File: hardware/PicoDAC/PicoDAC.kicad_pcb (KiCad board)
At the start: 4 copper layers, 38.6 x 73.3 mm, 48 parts, among them CN1 PJ-327A 5JJ, U1 CS43131-CNZR, U2 XIAO-RP2350-DIP, U3 PCA9306DCUR, U4 SN74AXC4T245PWR, U5 XTPS7A2018, U7 74AHCT1G125GV

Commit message: pcb rev 1.4, final touches
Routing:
- net VBUS: track 61.5 -> 75.5 mm, vias 0 -> 1
- net /USB_GND: track 13.4 -> 15.5 mm
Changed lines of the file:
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@@
 	)
 	(segment
+		(start 150.0227 149.157738)
+		(end 149.464162 148.5992)
+		(width 0.25)
+		(layer "B.Cu")
+		(net 1)
+	)
+	(segment
+		(start 149.464162 148.5992)
+		(end 149.2568 148.5992)
+		(width 0.25)
+		(layer "B.Cu")
+		(net 1)
+	)
+	(segment
+		(start 150.0227 150.219738)
+		(end 150.0227 149.157738)
+		(width 0.25)
+		(layer "B.Cu")
+		(net 1)
+	)
+	(segment
 		(start 156.922662 150.059738)
 		(end 157.3848 149.5976)
@@
 	(via
 		(at 148.25 115.61)
-		(size 0.3)
-		(drill 0.15)
+		(size 0.4)
+		(drill 0.2)
 		(layers "F.Cu" "B.Cu")
 		(net 27)
@@
 	(via
 		(at 149.479397 116.8786)
-		(size 0.3)
-		(drill 0.15)
+		(size 0.4)
+		(drill 0.2)
 		(layers "F.Cu" "B.Cu")
 		(net 27)
@@
 	(via
 		(at 148.229397 118.1286)
-		(size 0.3)
-		(drill 0.15)
+		(size 0.4)
+		(drill 0.2)
 		(layers "F.Cu" "B.Cu")
 		(net 27)
@@
 	(via
 		(at 148.229397 116.8786)
-		(size 0.3)
-		(drill 0.15)
+		(size 0.4)
+		(drill 0.2)
 		(layers "F.Cu" "B.Cu")
 		(net 27)
@@
 	(via
 		(at 149.479397 115.6286)
-		(size 0.3)
-		(drill 0.15)
+		(size 0.4)
+		(drill 0.2)
 		(layers "F.Cu" "B.Cu")
 		(net 27)
@@
 	(via
 		(at 150.729397 115.6286)
-		(size 0.3)
-		(drill 0.15)
+		(size 0.4)
+		(drill 0.2)
 		(layers "F.Cu" "B.Cu")
 		(net 27)
@@
 	(via
 		(at 149.479397 118.1286)
-		(size 0.3)
-		(drill 0.15)
+		(size 0.4)
+		(drill 0.2)
 		(layers "F.Cu" "B.Cu")
 		(net 27)
@@
 	(via
 		(at 150.729397 116.8786)
-		(size 0.3)
-		(drill 0.15)
+		(size 0.4)
+		(drill 0.2)
 		(layers "F.Cu" "B.Cu")
 		(net 27)
@@
 	(via
 		(at 150.729397 118.1286)
-		(size 0.3)
-		(drill 0.15)
+		(size 0.4)
+		(drill 0.2)
 		(layers "F.Cu" "B.Cu")
 		(net 27)
@@
 	)
 	(segment
+		(start 161.165763 88.775763)
+		(end 159.385 86.995)
+		(width 0.5)
+		(layer "F.Cu")
+		(net 68)
+	)
+	(segment
+		(start 162.358 88.775763)
+		(end 161.165763 88.775763)
+		(width 0.5)
+		(layer "F.Cu")
+		(net 68)
+	)
+	(segment
 		(start 161.2982 114.1026)
 		(end 161.2982 110.4882)
@@
 		(net 68)
 	)
+	(via
+		(at 159.385 86.995)
+		(size 0.6)
+		(drill 0.3)
+		(layers "F.Cu" "B.Cu")
+		(net 68)
+	)
+	(segment
+		(start 151.629453 82.804)
+		(end 151.587953 82.7625)
+		(width 1.25)
+		(layer "B.Cu")
+		(net 68)
+	)
+	(segment
+		(start 159.385 86.995)
+		(end 159.385 85.725)
+		(width 1.25)
+		(layer "B.Cu")
+		(net 68)
+	)
+	(segment
+		(start 159.385 85.725)
+		(end 156.464 82.804)
+		(width 1.25)
+		(layer "B.Cu")
+		(net 68)
+	)
+	(segment
+		(start 156.464 82.804)
+		(end 151.629453 82.804)
+		(width 1.25)
+		(layer "B.Cu")
+		(net 68)
+	)
 	(segment
 		(start 150.743053 99.6324)
@@
 	)
 	(zone
-		(net 44)
-		(net_name "/DAC_RESET")
+		(net 9)
+		(net_name "/LED_CONTROL")
 		(layer "F.Cu")
 		(name "$teardrop_padvia$")
 		(hatch none 0.1)
-		(priority 30000)
+		(priority 30005)
 		(attr
 			(teardrop
@@
 		(polygon
 			(pts
-				(xy 153.496991 94.400092) (xy 153.850545 94.046538) (xy 153.538953 93.01087) (xy 152.372246 92.921793)
-				(xy 152.057323 93.6845)
+				(xy 136.278545 81.638462) (xy 135.924991 81.284908) (xy 135.053536 82.0005) (xy 135.562246 82.763207)
+				(xy 136.684316 82.045137)
 			)
 		)
 	)
 	(zone
-		(net 9)
-		(net_name "/LED_CONTROL")
+		(net 44)
+		(net_name "/DAC_RESET")
 		(layer "F.Cu")
 		(name "$teardrop_padvia$")
 		(hatch none 0.1)
-		(priority 30004)
+		(priority 30000)
 		(attr
 			(teardrop
@@
 		(polygon
 			(pts
-				(xy 136.278545 81.638462) (xy 135.924991 81.284908) (xy 135.053536 82.0005) (xy 135.562246 82.763207)
-				(xy 136.684316 82.045137)
+				(xy 153.496991 94.400092) (xy 153.850545 94.046538) (xy 153.538953 93.01087) (xy 152.372246 92.921793)
+				(xy 152.057323 93.6845)
 			)
 		)
 	)
 	(zone
-		(net 9)
-		(net_name "/LED_CONTROL")
+		(net 65)
+		(net_name "/MCU_GP_00")
 		(layer "F.Cu")
 		(name "$teardrop_padvia$")
 		(hatch none 0.1)
-		(priority 30005)
+		(priority 30006)
 		(attr
 			(teardrop
@@
 		(polygon
 			(pts
-				(xy 136.278545 81.638462) (xy 135.924991 81.284908) (xy 135.053536 82.0005) (xy 135.562246 82.763207)
-				(xy 136.684316 82.045137)
+				(xy 135.925859 99.426235) (xy 136.102635 99.249459) (xy 136.621667 98.755525) (xy 135.562246 98.001793)
+				(xy 135.015851 98.7645)
 			)
 		)
 	)
 	(zone
-		(net 65)
-		(net_name "/MCU_GP_00")
+		(net 45)
+		(net_name "/LS1_1OE")
 		(layer "F.Cu")
 		(name "$teardrop_padvia$")
 		(hatch none 0.1)
-		(priority 30006)
+		(priority 30002)
 		(attr
 			(teardrop
@@
 		(polygon
 			(pts
-				(xy 135.925859 99.426235) (xy 136.102635 99.249459) (xy 136.621667 98.755525) (xy 135.562246 98.001793)
-				(xy 135.015851 98.7645)
+				(xy 133.571489 90.354283) (xy 133.748264 90.531058) (xy 134.44159 91.099863) (xy 135.56366 90.381793)
+				(xy 134.44159 89.665137)
 			)
 		)
 	)
 	(zone
-		(net 45)
-		(net_name "/LS1_1OE")
+		(net 9)
+		(net_name "/LED_CONTROL")
 		(layer "F.Cu")
 		(name "$teardrop_padvia$")
 		(hatch none 0.1)
-		(priority 30002)
+		(priority 30004)
 		(attr
 			(teardrop
@@
 		(polygon
 			(pts
-				(xy 133.571489 90.354283) (xy 133.748264 90.531058) (xy 134.44159 91.099863) (xy 135.56366 90.381793)
-				(xy 134.44159 89.665137)
+				(xy 136.278545 81.638462) (xy 135.924991 81.284908) (xy 135.053536 82.0005) (xy 135.562246 82.763207)
+				(xy 136.684316 82.045137)
 			)
 		)

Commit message: rev 1.5
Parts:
- moved U2 1.24 mm to (145.2, 90.3)
- moved R9 0.58 mm to (165.5, 84.5), turned to -90 degrees
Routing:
- net VBUS: track 75.5 -> 72.9 mm
- net /DAC_RESET: track 25.3 -> 22.7 mm
- net /LS1_1OE: track 39.1 -> 37.0 mm
- net /MCU_GP_02: track 17.2 -> 19.2 mm
- net /MCU_GP_06: track 29.4 -> 27.8 mm
- net /LED_CONTROL: track 34.1 -> 32.7 mm
- net /MCU_GP_07: track 29.8 -> 28.6 mm
- net Net-(LED1-DIN): track 5.07 -> 3.89 mm
- net +3.3V: track 90.6 -> 91.5 mm
- net /MCU_GP_01: track 18.1 -> 19.0 mm
- net /MCU_GP_03: track 29.0 -> 29.5 mm
- net /MCU_GP_00: track 8.72 -> 8.22 mm
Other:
- board size 38.6 x 73.3 mm -> 35.1 x 73.3 mm

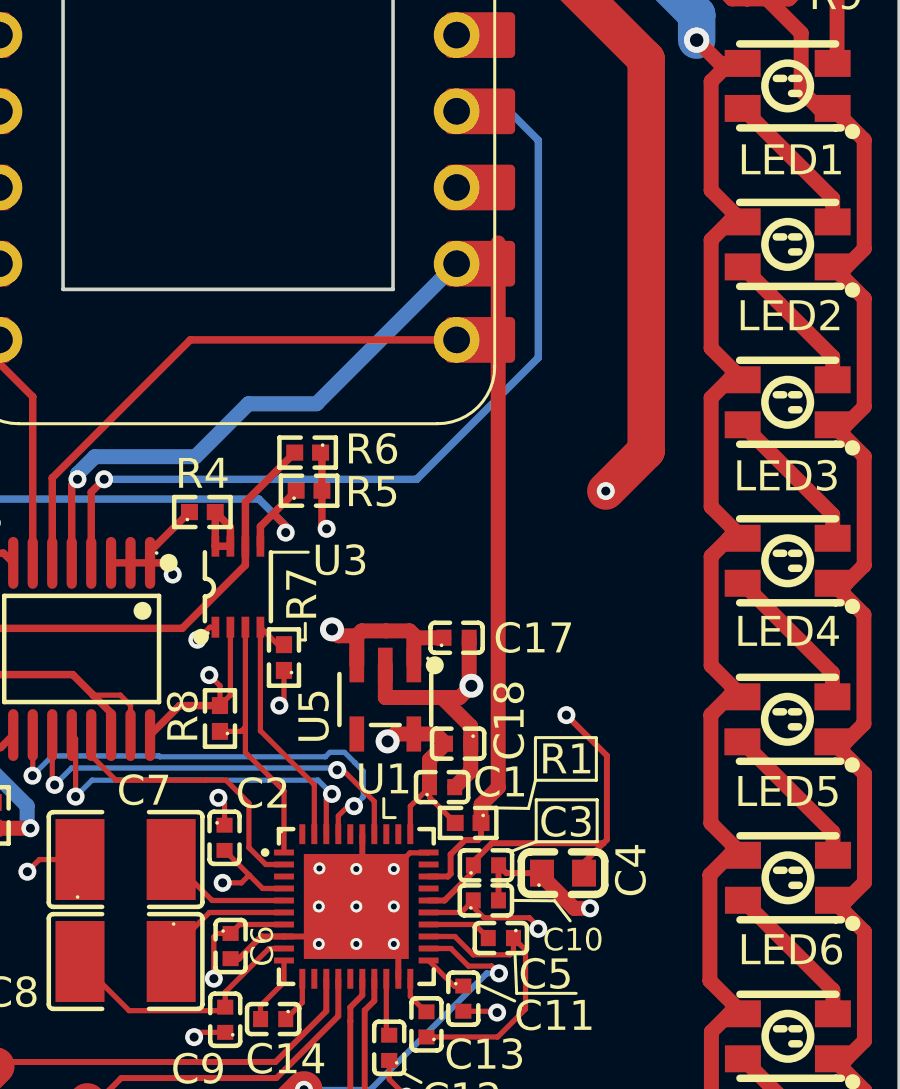
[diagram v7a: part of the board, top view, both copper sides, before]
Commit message: fixed floating xto pin
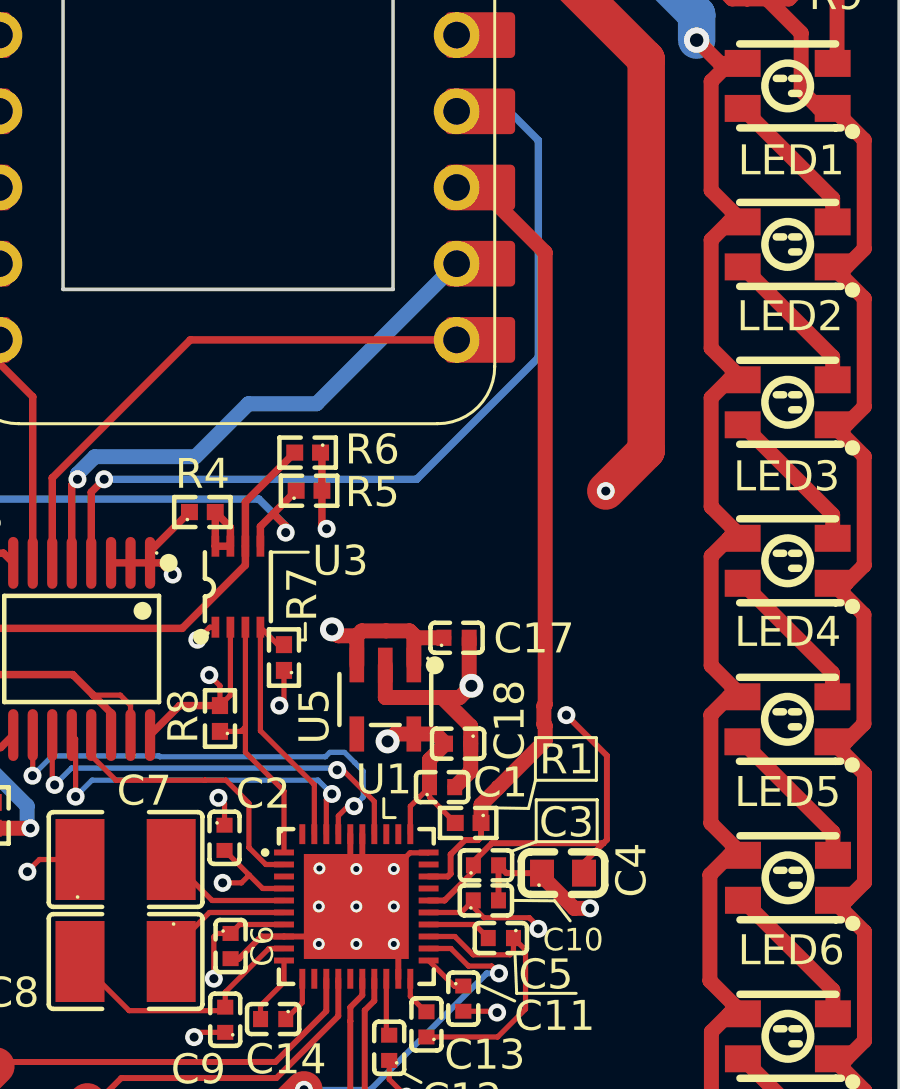
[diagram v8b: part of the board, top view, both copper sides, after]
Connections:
- U1 pad 36: unconnected-(U1-XTO-Pad36) -> GND
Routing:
- net /DAC_RESET: track 22.7 -> 26.1 mm
- net GND: track 129.9 -> 132.4 mm
